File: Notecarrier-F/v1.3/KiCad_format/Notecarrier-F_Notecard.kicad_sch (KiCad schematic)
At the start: 21 parts, among them J11 CES-102-01-S-S, J5 SF72S006VBDR2500, J6 MDT420E01001, SW1 CJS-1200TA, SW2 EVP-BB2A9B000

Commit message: Upgrade the four original ports to KiCad 9; fix F v1.3 DRC; document F errata
Notecarrier-A v2.0, -B v2.1, -F v1.3 and -Pi v1.1 were authored in KiCad 7 and
are now upgraded in place (board 20221018 -> 20241229, schematics -> 20250114).
The upgrade is verified lossless on all four:

- every fabrication layer (copper, mask, paste, silk, Edge.Cuts) is
  geometrically identical before and after at 600 dpi, and drill files are
  textually identical;
- schematic netlists are unchanged - same components, same net partitions
  (A 99/114, B 62/87, F 110/166, Pi 46/95);
- kicanvas renders and the RAG extract both still pass.

Zones are NOT refilled - these ports depend on preserved fills.

Notecarrier-F: the board's 54 net-less 0.6 mm copper patches (footprint
weird-no-fill-via_Fv1.2) sit inside GND copper and are now assigned the GND net
they belong to. DRC goes from 171 errors to 0 with no change to any copper
geometry.

Notecarrier-F ERRATA.md (new): the power section does not match the shipped
board. U9 (AP2139AK-3.3 LDO) with C33/C34, and DS7 (STPS3H100U), are missing
from both schematic and board though they are in the Altium source, the released
BOM, the released pick-and-place, and the shipped copper/mask/paste. All six
diodes carry the wrong part and package: the released design uses FSV1045V in
TO277-3 (3 pads) for DS1/DS2/DS4/DS5 and STPS3H100U in SMB for DS3/DS6/DS7,
where the port has B360A-13-F in DO-214AC SMA (2 pads) throughout. The errata
records the exact wiring and coordinates needed to fix it. Flagged in the root
README and the port's README.

Also documented per port: the DRC exclusions recorded by KiCad 7 no longer
suppress anything, because KiCad 9 computes different marker keys. They are left
as the author's record and the remaining violations are explained in each
Porting-Notes - including evidence that A's J9 pad-vs-zone reports are
preserved-fill artifacts (its In1 plane matches the shipped GND film to within
0.9% of lit area), and that B's 4 error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
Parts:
- renumbered C3 to C5, C3 to C6, C3 to C7, C3 to C8, C3 to C9, R16 to R6, R5 to R7, R5 to R8, R5 to R9

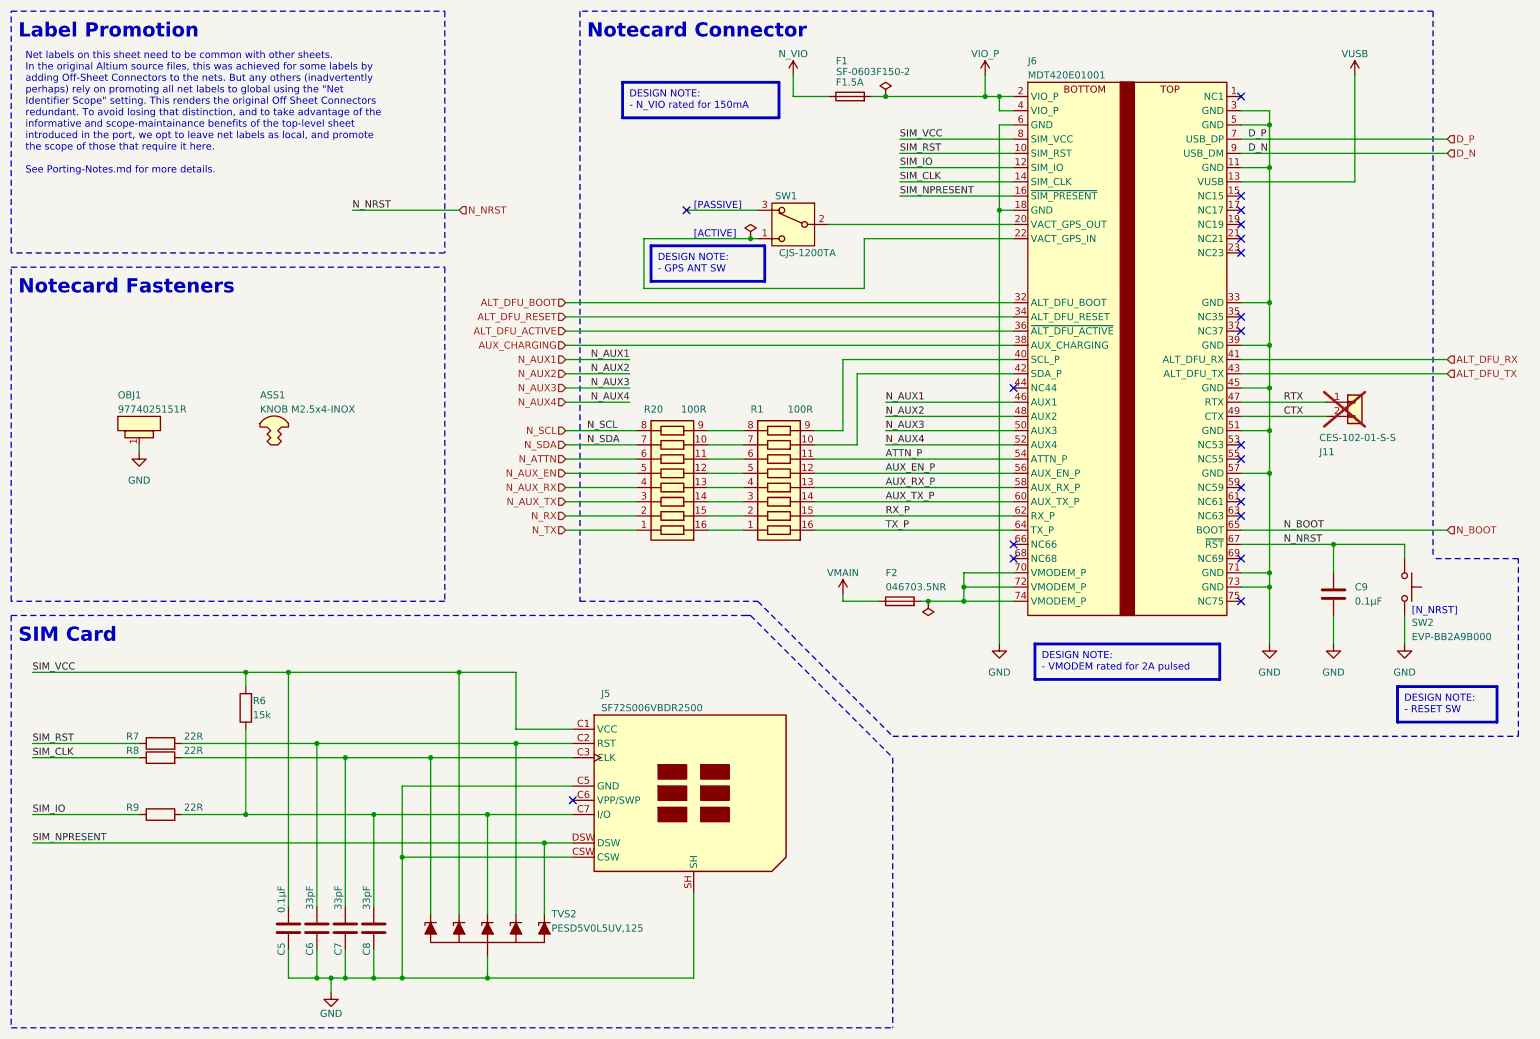
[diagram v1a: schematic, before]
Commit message: Notecarrier-F: convert its design-note text_boxes too
The first conversion pass scoped by red-frame rectangles and missed
Notecarrier-F: its 16 notes have no separate frame - the text_box itself draws
a 0.5mm red border - so they were entirely invisible on the published pages,
frames included. Same conversion as 25a2d84, with two additions the F notes
forced:

- KiCad's hidden PDF text layer mangles special glyphs (broken ToUnicode maps
  for u/~/ohm produce mojibake) and F's notes are full of them, so exact
  word-matching is unattainable. Notes whose visual line count matches their
  source line count need no wrap-freezing at all and are kept verbatim, guarded
  by a per-line ASCII similarity check; only genuinely wrapped notes use the
  strict word-level path, and F's wrapped notes are clean of special glyphs.
  The converter also now rebuilds output from SOURCE words - the PDF only
  supplies break positions - so KiCad markup like R_{iset} stays markup in the
  file instead of being replaced by its rendered form.

- The F author gave these notes an explicit black font color. Black is what
  KiCad plots either way, but explicit black is invisible on a dark-theme
  viewer. The 16 notes now carry no explicit color, like every other board's
  notes: KiCad plots its default dark blue, kicanvas its theme color. This is
  the one deliberate visual change - note text black -> dark blue in KiCad -
  and it makes F consistent with the other five boards.

Netlist byte-equal before and after; kicanvas renders all four modified sheets
with the notes visible and the subscript markup intact.

Co-Authored-By: Claude Fable 5 <noreply@anthropic.com>
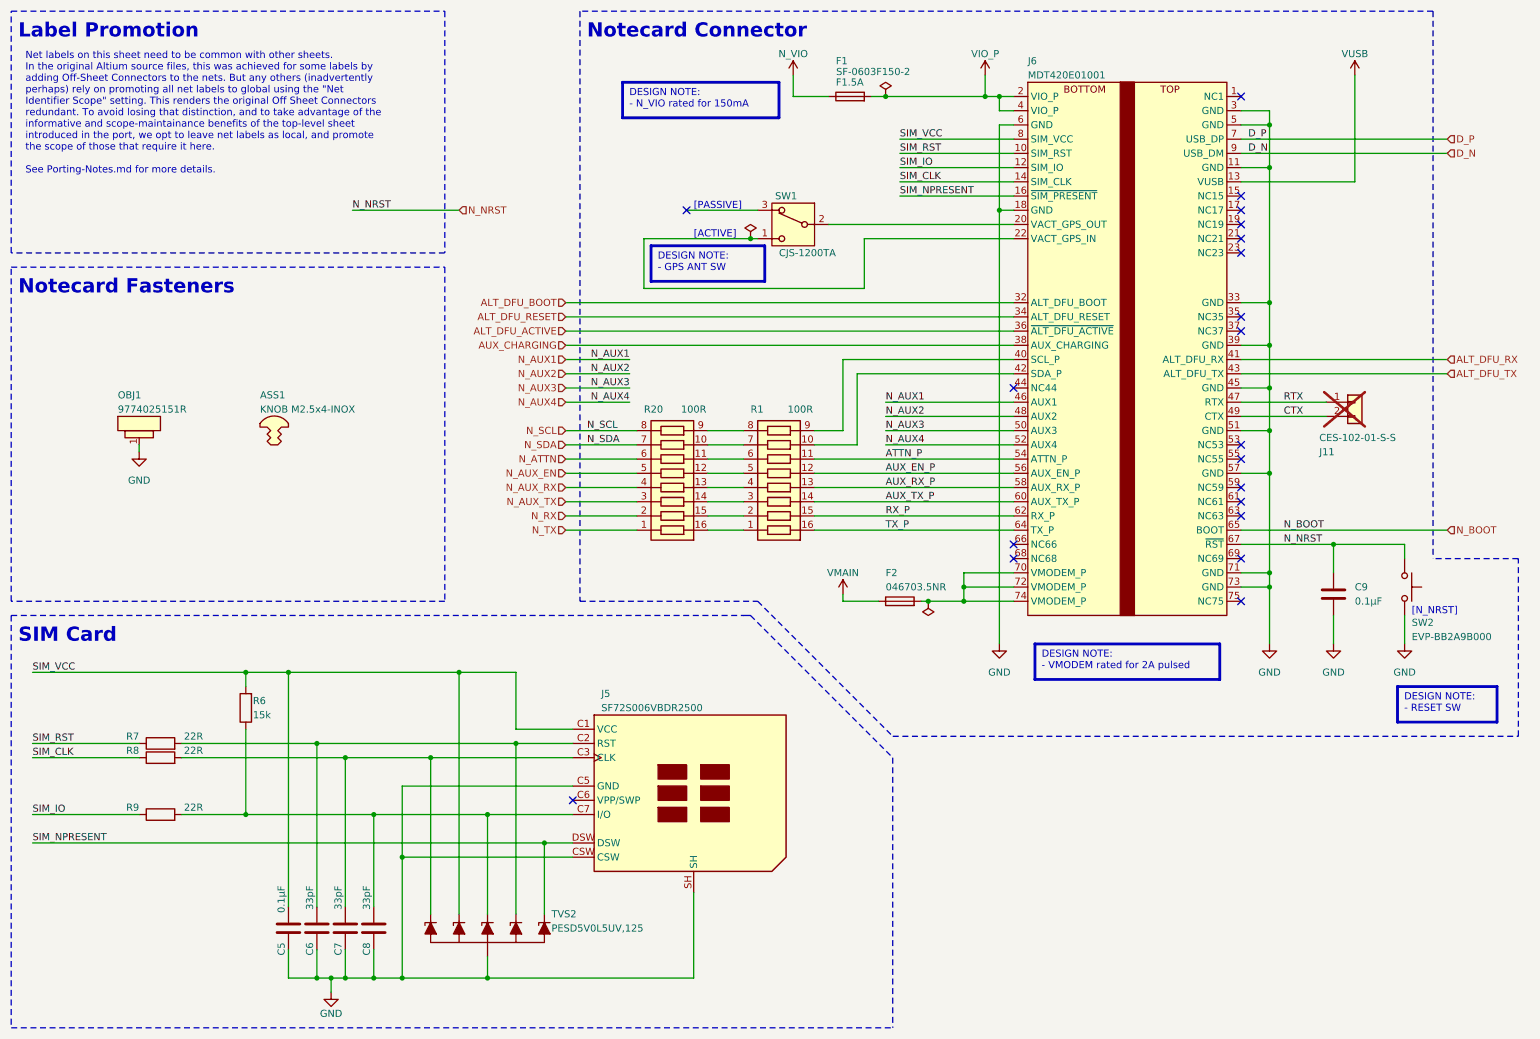
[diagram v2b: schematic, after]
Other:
- note added: "DESIGN NOTE: - GPS ANT SW"
- note added: "DESIGN NOTE: - N_VIO rated for 150mA"
- note added: "DESIGN NOTE: - RESET SW"
- note added: "DESIGN NOTE: - VMODEM rated for 2A pulsed"
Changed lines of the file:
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@@
 		)
 	)
-	(text_box "DESIGN NOTE:\n- GPS ANT SW"
-		(exclude_from_sim no)
-		(at 128.27 55.88 0)
-		(size 20.32 6.35)
-		(margins 1.2025 1.2025 1.2025 1.2025)
+	(rectangle
+		(start 128.27 55.88)
+		(end 148.59 62.23)
 		(stroke
 			(width 0.5)
@@
 			(type none)
 		)
+	)
+	(text "DESIGN NOTE:\n- GPS ANT SW"
+		(exclude_from_sim no)
+		(at 129.472 57.0825 0)
 		(effects
 			(font
 				(size 1.27 1.27)
-				(color 0 0 0 1)
 			)
 			(justify left top)
 		)
 	)
-	(text_box "DESIGN NOTE:\n- VMODEM rated for 2A pulsed"
-		(exclude_from_sim no)
-		(at 196.85 127 0)
-		(size 33.02 6.35)
-		(margins 1.2025 1.2025 1.2025 1.2025)
+	(rectangle
+		(start 196.85 127)
+		(end 229.87 133.35)
 		(stroke
 			(width 0.5)
@@
 			(type none)
 		)
+	)
+	(text "DESIGN NOTE:\n- VMODEM rated for 2A pulsed"
+		(exclude_from_sim no)
+		(at 198.052 128.202 0)
 		(effects
 			(font
 				(size 1.27 1.27)
-				(color 0 0 0 1)
 			)
 			(justify left top)
 		)
 	)
-	(text_box "DESIGN NOTE:\n- N_VIO rated for 150mA"
-		(exclude_from_sim no)
-		(at 123.19 26.67 0)
-		(size 27.94 6.35)
-		(margins 1.2025 1.2025 1.2025 1.2025)
+	(rectangle
+		(start 123.19 26.67)
+		(end 151.13 33.02)
 		(stroke
 			(width 0.5)
@@
 			(type none)
 		)
+	)
+	(text "DESIGN NOTE:\n- N_VIO rated for 150mA"
+		(exclude_from_sim no)
+		(at 124.392 27.8725 0)
 		(effects
 			(font
 				(size 1.27 1.27)
-				(color 0 0 0 1)
 			)
 			(justify left top)
 		)
 	)
-	(text_box "DESIGN NOTE:\n- RESET SW"
-		(exclude_from_sim no)
-		(at 261.62 134.62 0)
-		(size 17.78 6.35)
-		(margins 1.2025 1.2025 1.2025 1.2025)
+	(rectangle
+		(start 261.62 134.62)
+		(end 279.4 140.97)
 		(stroke
 			(width 0.5)
@@
 			(type none)
 		)
+	)
+	(text "DESIGN NOTE:\n- RESET SW"
+		(exclude_from_sim no)
+		(at 262.822 135.822 0)
 		(effects
 			(font
 				(size 1.27 1.27)
-				(color 0 0 0 1)
 			)
 			(justify left top)
